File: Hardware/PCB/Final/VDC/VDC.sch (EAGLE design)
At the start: 76 parts, among them U1 IL300, U10 IL300, U11 MCP602-E/P, U12 MCP602-E/P, U13 AD7993BRUZ-0, U2 MCP602-E/P, U3 MCP602-E/P, U4 IL300, U5 MCP602-E/P, U6 MCP602-E/P, U7 IL300, U8 MCP602-E/P, U9 MCP602-E/P

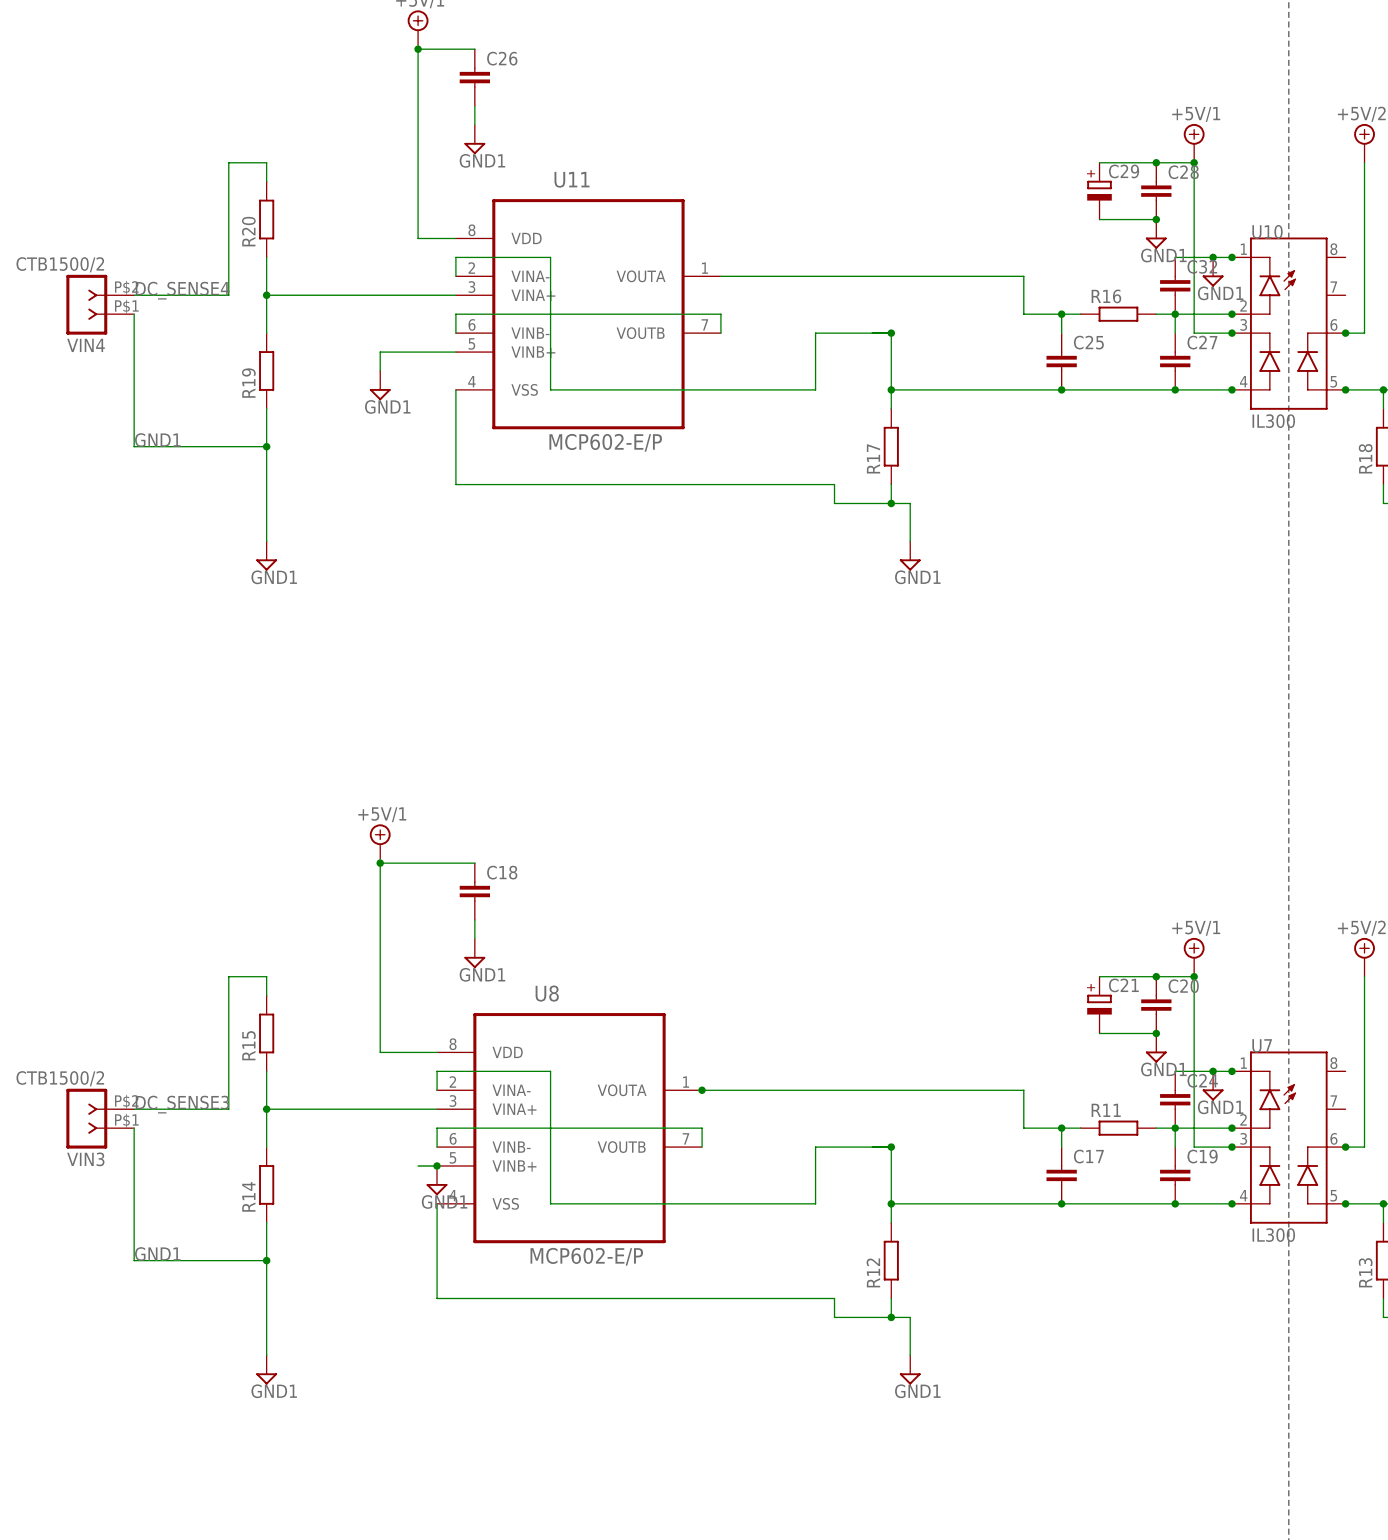
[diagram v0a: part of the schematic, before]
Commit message: Made changes to the PCB Folders
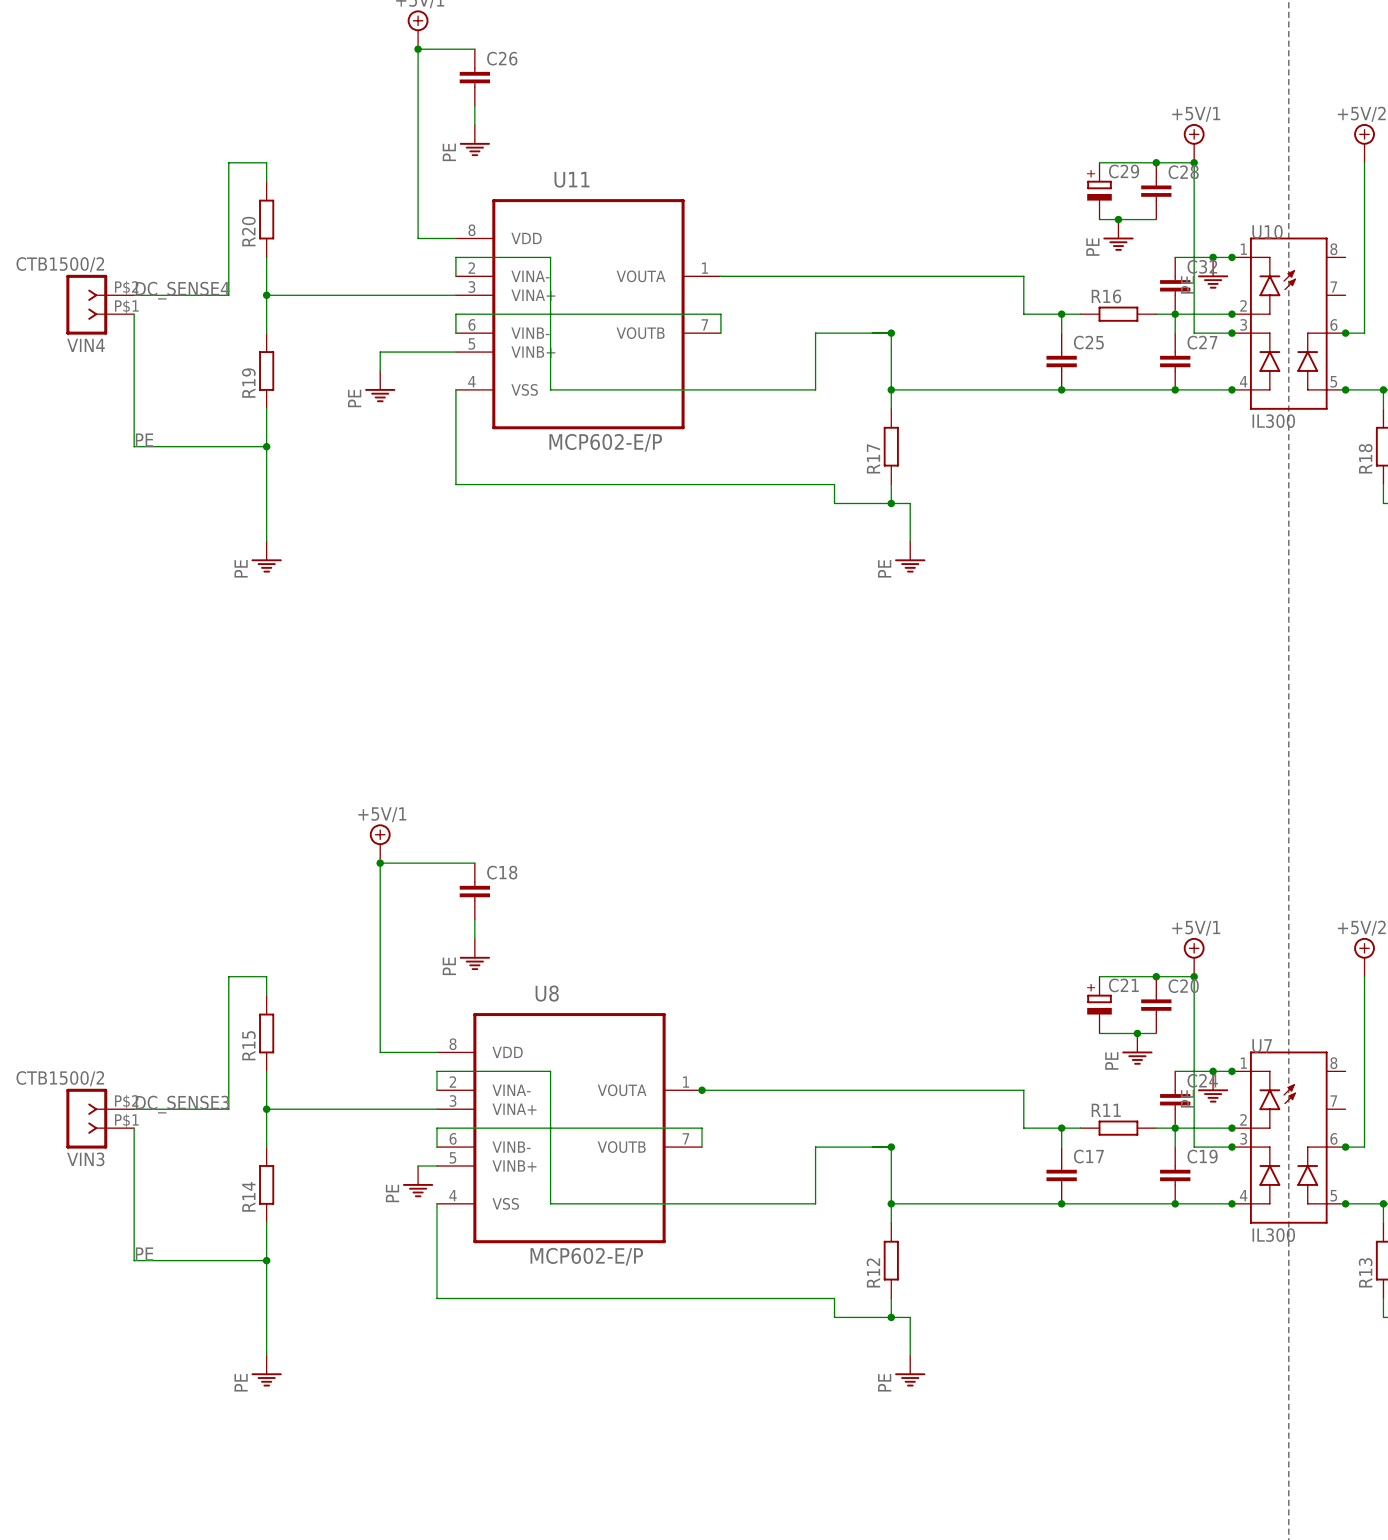
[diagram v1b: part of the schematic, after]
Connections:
- new net PE: C18.2, C20.2, C21.-, C24.1, C26.2, C28.2, C29.-, C32.1, R12.1, R14.1, R17.1, R19.1, U10.C_LED, U11.VINB+, U11.VSS, U7.C_LED, U8.VINB+, U8.VSS, VIN3.1, VIN4.1
- net GND1: no longer C18.2, C20.2, C21.-, C24.1, C26.2, C28.2, C29.-, C32.1, R12.1, R14.1, R17.1, R19.1, U10.C_LED, U11.VINB+, U11.VSS, U7.C_LED, U8.VINB+, U8.VSS, VIN3.1, VIN4.1
